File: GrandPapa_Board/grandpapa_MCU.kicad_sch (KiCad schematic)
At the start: 25 parts, among them J6 Conn_02x06, U10 MCP2515, U7 MCP2562, U8 MCP2562, U9 PIC18F26K83, Y1 12MHz

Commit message: minor changes, change some buck converter component values, add inductor + LED part numbers
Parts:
- R13, R15: value 470R -> 100R
- R14: value 470R -> 150R
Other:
- note added: "Debugging LEDs Vs = 5V"
- note added: "Vf = 2V @ 20mA"
- note added: "Vf = 3.2V @ 20mA"
- note added: "Vf = 3.3V @ 20mA"
- note removed: "Debugging LEDs Vs = 3.3V"
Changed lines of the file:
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@@
     (stroke (width 0) (type default) (color 0 0 0 0))
+  )
+  (text "Vf = 3.2V @ 20mA" (at 205.105 144.145 0)
+    (effects (font (size 1.27 1.27)) (justify left bottom))
+  )
+  (text "Vf = 3.3V @ 20mA" (at 153.67 154.305 0)
+    (effects (font (size 1.27 1.27)) (justify left bottom))
   )
   (text "See Table 3 in datasheet for pin allocation table\n"
@@
     (effects (font (size 1.27 1.27)) (justify left bottom))
   )
+  (text "Vf = 2V @ 20mA" (at 177.8 146.685 0)
+    (effects (font (size 1.27 1.27)) (justify left bottom))
+  )
   (text "WHITE\n" (at 153.67 147.32 0)
     (effects (font (size 1.27 1.27)) (justify left bottom))
   )
-  (text "Debugging LEDs\nVs = 3.3V\n" (at 169.545 158.75 0)
+  (text "Debugging LEDs\nVs = 5V\n" (at 170.18 162.56 0)
     (effects (font (size 1.27 1.27)) (justify left bottom))
   )
@@
       (effects (font (size 1.27 1.27)) (justify left))
     )
-    (property "Value" "470R" (id 1) (at 176.3522 134.493 0)
+    (property "Value" "150R" (id 1) (at 176.3522 134.493 0)
       (effects (font (size 1.27 1.27)) (justify left))
     )
@@
       (effects (font (size 1.27 1.27)) (justify left))
     )
-    (property "Value" "470R" (id 1) (at 152.2222 140.843 0)
+    (property "Value" "100R" (id 1) (at 152.2222 140.843 0)
       (effects (font (size 1.27 1.27)) (justify left))
     )
@@
       (effects (font (size 1.27 1.27)) (justify left))
     )
-    (property "Value" "470R" (id 1) (at 203.6572 131.953 0)
-      (effects (font (size 1.27 1.27)) (justify left))
-    )
+    (property "Value" "100R" (id 1) (at 203.6572 131.953 0)
+      (effects (font (size 1.27 1.27)) (justify left))
+    )

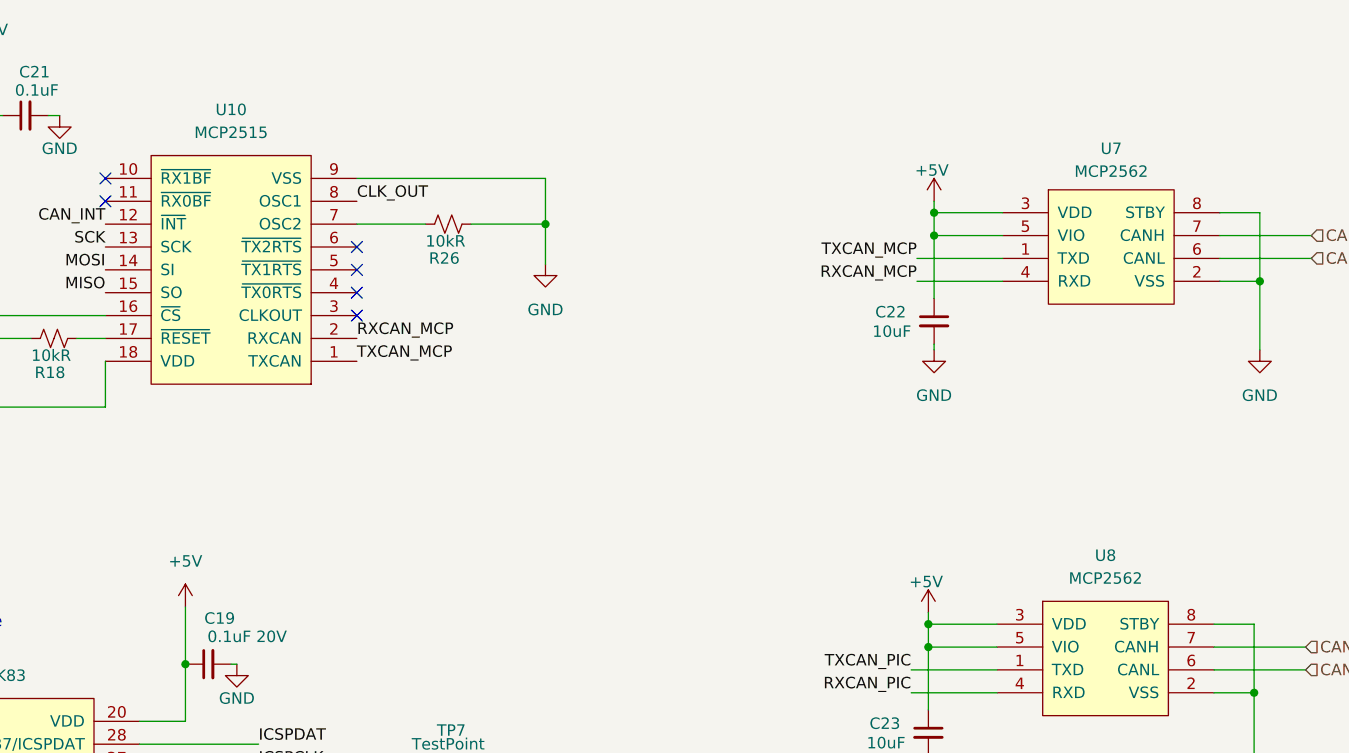
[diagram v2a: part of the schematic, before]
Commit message: Add footprints, inductors TBD
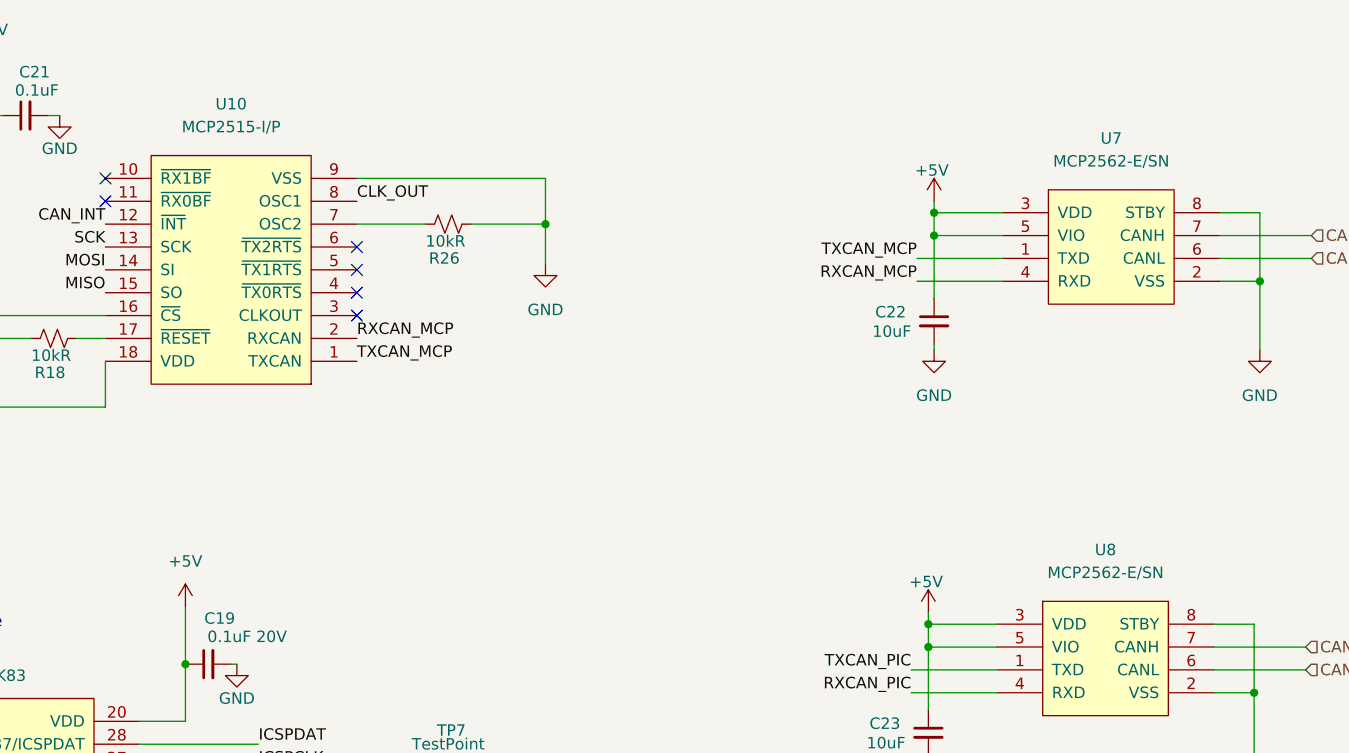
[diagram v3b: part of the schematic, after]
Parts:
- C18, C19, C21, C22, C23: footprint (none) -> Capacitor_SMD:C_0805_2012Metric_Pad1.18x1.45mm_HandSolder
- R11, R12, R17, R18, R26: footprint (none) -> Resistor_SMD:R_0805_2012Metric_Pad1.20x1.40mm_HandSolder
- TP7: footprint (none) -> Connector_PinHeader_2.54mm:PinHeader_1x01_P2.54mm_Vertical
- U10: value MCP2515 -> MCP2515-I/P; footprint (none) -> Package_SO:SOIC-18W_7.5x11.6mm_P1.27mm
- U7, U8: value MCP2562 -> MCP2562-E/SN; footprint (none) -> Package_SO:SOIC-8_3.9x4.9mm_P1.27mm
- U9: footprint (none) -> GrandPapa:SOIC127P1030X265-28N
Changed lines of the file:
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@@
       (effects (font (size 1.27 1.27)) (justify left))
     )
-    (property "Footprint" "" (id 2) (at 161.29 47.625 0)
+    (property "Footprint" "Resistor_SMD:R_0805_2012Metric_Pad1.20x1.40mm_HandSolder" (id 2) (at 161.29 47.625 0)
       (effects (font (size 1.27 1.27)) hide)
     )
@@
     (property "Reference" "C23" (id 0) (at 209.804 103.124 0))
     (property "Value" "10uF" (id 1) (at 209.931 105.283 0))
-    (property "Footprint" "" (id 2) (at 214.63 104.14 0)
+    (property "Footprint" "Capacitor_SMD:C_0805_2012Metric_Pad1.18x1.45mm_HandSolder" (id 2) (at 214.63 104.14 0)
       (effects (font (size 1.27 1.27)) hide)
     )
@@
     (property "Reference" "C22" (id 0) (at 210.439 57.404 0))
     (property "Value" "10uF" (id 1) (at 210.566 59.563 0))
-    (property "Footprint" "" (id 2) (at 215.265 58.42 0)
+    (property "Footprint" "Capacitor_SMD:C_0805_2012Metric_Pad1.18x1.45mm_HandSolder" (id 2) (at 215.265 58.42 0)
       (effects (font (size 1.27 1.27)) hide)
     )
@@
       (effects (font (size 1.27 1.27)) (justify left))
     )
-    (property "Footprint" "" (id 2) (at 48.895 108.585 0)
+    (property "Footprint" "Capacitor_SMD:C_0805_2012Metric_Pad1.18x1.45mm_HandSolder" (id 2) (at 48.895 108.585 0)
       (effects (font (size 1.27 1.27)) hide)
     )
@@
     (property "Reference" "C21" (id 0) (at 115.316 30.734 90))
     (property "Value" "0.1uF" (id 1) (at 115.57 32.766 90))
-    (property "Footprint" "" (id 2) (at 114.3 35.56 0)
+    (property "Footprint" "Capacitor_SMD:C_0805_2012Metric_Pad1.18x1.45mm_HandSolder" (id 2) (at 114.3 35.56 0)
       (effects (font (size 1.27 1.27)) hide)
     )
@@
       (effects (font (size 1.27 1.27)) (justify left))
     )
-    (property "Footprint" "" (id 2) (at 117.475 60.325 0)
+    (property "Footprint" "Resistor_SMD:R_0805_2012Metric_Pad1.20x1.40mm_HandSolder" (id 2) (at 117.475 60.325 0)
       (effects (font (size 1.27 1.27)) hide)
     )
@@
     (property "Reference" "R12" (id 0) (at 55.88 98.806 90))
     (property "Value" "100R" (id 1) (at 55.88 100.584 90))
-    (property "Footprint" "" (id 2) (at 55.88 102.87 0)
+    (property "Footprint" "Resistor_SMD:R_0805_2012Metric_Pad1.20x1.40mm_HandSolder" (id 2) (at 55.88 102.87 0)
       (effects (font (size 1.27 1.27)) hide)
     )
@@
     (property "Reference" "C19" (id 0) (at 135.89 91.44 90))
     (property "Value" "0.1uF 20V" (id 1) (at 138.938 93.472 90))
-    (property "Footprint" "" (id 2) (at 134.62 96.52 0)
+    (property "Footprint" "Capacitor_SMD:C_0805_2012Metric_Pad1.18x1.45mm_HandSolder" (id 2) (at 134.62 96.52 0)
       (effects (font (size 1.27 1.27)) hide)
     )
@@
   (symbol (lib_id "CANHW:MCP2515") (at 137.16 57.785 180) (unit 1)
     (in_bom yes) (on_board yes) (fields_autoplaced)
-    (property "Reference" "U10" (id 0) (at 137.16 34.925 0))
-    (property "Value" "MCP2515" (id 1) (at 137.16 37.465 0))
-    (property "Footprint" "" (id 2) (at 138.43 57.785 0)
+    (property "Reference" "U10" (id 0) (at 137.16 34.29 0))
+    (property "Value" "MCP2515-I/P" (id 1) (at 137.16 36.83 0))
+    (property "Footprint" "Package_SO:SOIC-18W_7.5x11.6mm_P1.27mm" (id 2) (at 138.43 57.785 0)
       (effects (font (size 1.27 1.27)) hide)
     )
@@
   (symbol (lib_id "CANHW:MCP2562") (at 235.585 46.355 0) (unit 1)
     (in_bom yes) (on_board yes) (fields_autoplaced)
-    (property "Reference" "U7" (id 0) (at 234.95 39.243 0))
-    (property "Value" "MCP2562" (id 1) (at 234.95 41.783 0))
-    (property "Footprint" "" (id 2) (at 235.585 46.355 0)
+    (property "Reference" "U7" (id 0) (at 234.95 38.1 0))
+    (property "Value" "MCP2562-E/SN" (id 1) (at 234.95 40.64 0))
+    (property "Footprint" "Package_SO:SOIC-8_3.9x4.9mm_P1.27mm" (id 2) (at 235.585 46.355 0)
       (effects (font (size 1.27 1.27)) hide)
     )
@@
   (symbol (lib_id "CANHW:MCP2562") (at 234.95 92.075 0) (unit 1)
     (in_bom yes) (on_board yes) (fields_autoplaced)
-    (property "Reference" "U8" (id 0) (at 234.315 84.455 0))
-    (property "Value" "MCP2562" (id 1) (at 234.315 86.995 0))
-    (property "Footprint" "" (id 2) (at 234.95 92.075 0)
+    (property "Reference" "U8" (id 0) (at 234.315 83.82 0))
+    (property "Value" "MCP2562-E/SN" (id 1) (at 234.315 86.36 0))
+    (property "Footprint" "Package_SO:SOIC-8_3.9x4.9mm_P1.27mm" (id 2) (at 234.95 92.075 0)
       (effects (font (size 1.27 1.27)) hide)
     )
@@
       (effects (font (size 1.27 1.27)) (justify left))
     )
-    (property "Footprint" "" (id 2) (at 105.41 50.165 0)
+    (property "Footprint" "Resistor_SMD:R_0805_2012Metric_Pad1.20x1.40mm_HandSolder" (id 2) (at 105.41 50.165 0)
       (effects (font (size 1.27 1.27)) hide)
     )
@@
     (property "Reference" "U9" (id 0) (at 108.585 95.25 0))
     (property "Value" "PIC18F26K83" (id 1) (at 108.585 97.79 0))
-    (property "Footprint" "" (id 2) (at 120.65 119.38 0)
+    (property "Footprint" "GrandPapa:SOIC127P1030X265-28N" (id 2) (at 120.65 119.38 0)
       (effects (font (size 1.27 1.27)) hide)
     )
@@
       (effects (font (size 1.27 1.27)) (justify left))
     )
-    (property "Footprint" "" (id 2) (at 166.37 110.49 0)
+    (property "Footprint" "Connector_PinHeader_2.54mm:PinHeader_1x01_P2.54mm_Vertical" (id 2) (at 166.37 110.49 0)
       (effects (font (size 1.27 1.27)) hide)
     )
@@
       (effects (font (size 1.27 1.27)) (justify left))
     )
-    (property "Footprint" "" (id 2) (at 46.355 96.52 0)
-      (effects (font (size 1.27 1.27)) hide)
-    )
+    (property "Footprint" "Resistor_SMD:R_0805_2012Metric_Pad1.20x1.40mm_HandSolder" (id 2) (at 46.355 96.52 0)
+      (effects (font (size 1.27 1.27)) hide)
+    )

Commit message: Finish footprints, add board outline
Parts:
- U9: footprint GrandPapa:SOIC127P1030X265-28N -> Package_SO:SSOP-28_5.3x10.2mm_P0.65mm
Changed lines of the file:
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@@
     (property "Reference" "U9" (id 0) (at 108.585 95.25 0))
     (property "Value" "PIC18F26K83" (id 1) (at 108.585 97.79 0))
-    (property "Footprint" "GrandPapa:SOIC127P1030X265-28N" (id 2) (at 120.65 119.38 0)
+    (property "Footprint" "Package_SO:SSOP-28_5.3x10.2mm_P0.65mm" (id 2) (at 120.65 119.38 0)
       (effects (font (size 1.27 1.27)) hide)
     )

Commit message: update layout + routing
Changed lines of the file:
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@@
     (effects (font (size 1.27 1.27)) (justify right bottom))
-  )
-  (hierarchical_label "CANL_ROCKET" (shape input) (at 256.54 97.155 0)
-    (effects (font (size 1.27 1.27)) (justify left))
-  )
-  (hierarchical_label "CANH_ROCKET" (shape input) (at 256.54 94.615 0)
-    (effects (font (size 1.27 1.27)) (justify left))
   )
   (hierarchical_label "VBATT_VOLT_SENSE" (shape input) (at 87.63 113.03 180)
@@
   )
   (hierarchical_label "BATT_CHARGER_PG" (shape input) (at 127 118.11 0)
+    (effects (font (size 1.27 1.27)) (justify left))
+  )
+  (hierarchical_label "CANL_ROCKET" (shape input) (at 256.5367 97.155 0)
     (effects (font (size 1.27 1.27)) (justify left))
   )
@@
     (effects (font (size 1.27 1.27)) (justify right))
   )
+  (hierarchical_label "CANH_ROCKET" (shape input) (at 256.54 94.615 0)
+    (effects (font (size 1.27 1.27)) (justify left))
+  )
   (hierarchical_label "CANH_PAYLOAD" (shape input) (at 257.175 48.895 0)
